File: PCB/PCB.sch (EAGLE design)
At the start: 216 parts, among them J3 Boot, Q1 FS8205A, U1 ESP32-S3HOLE

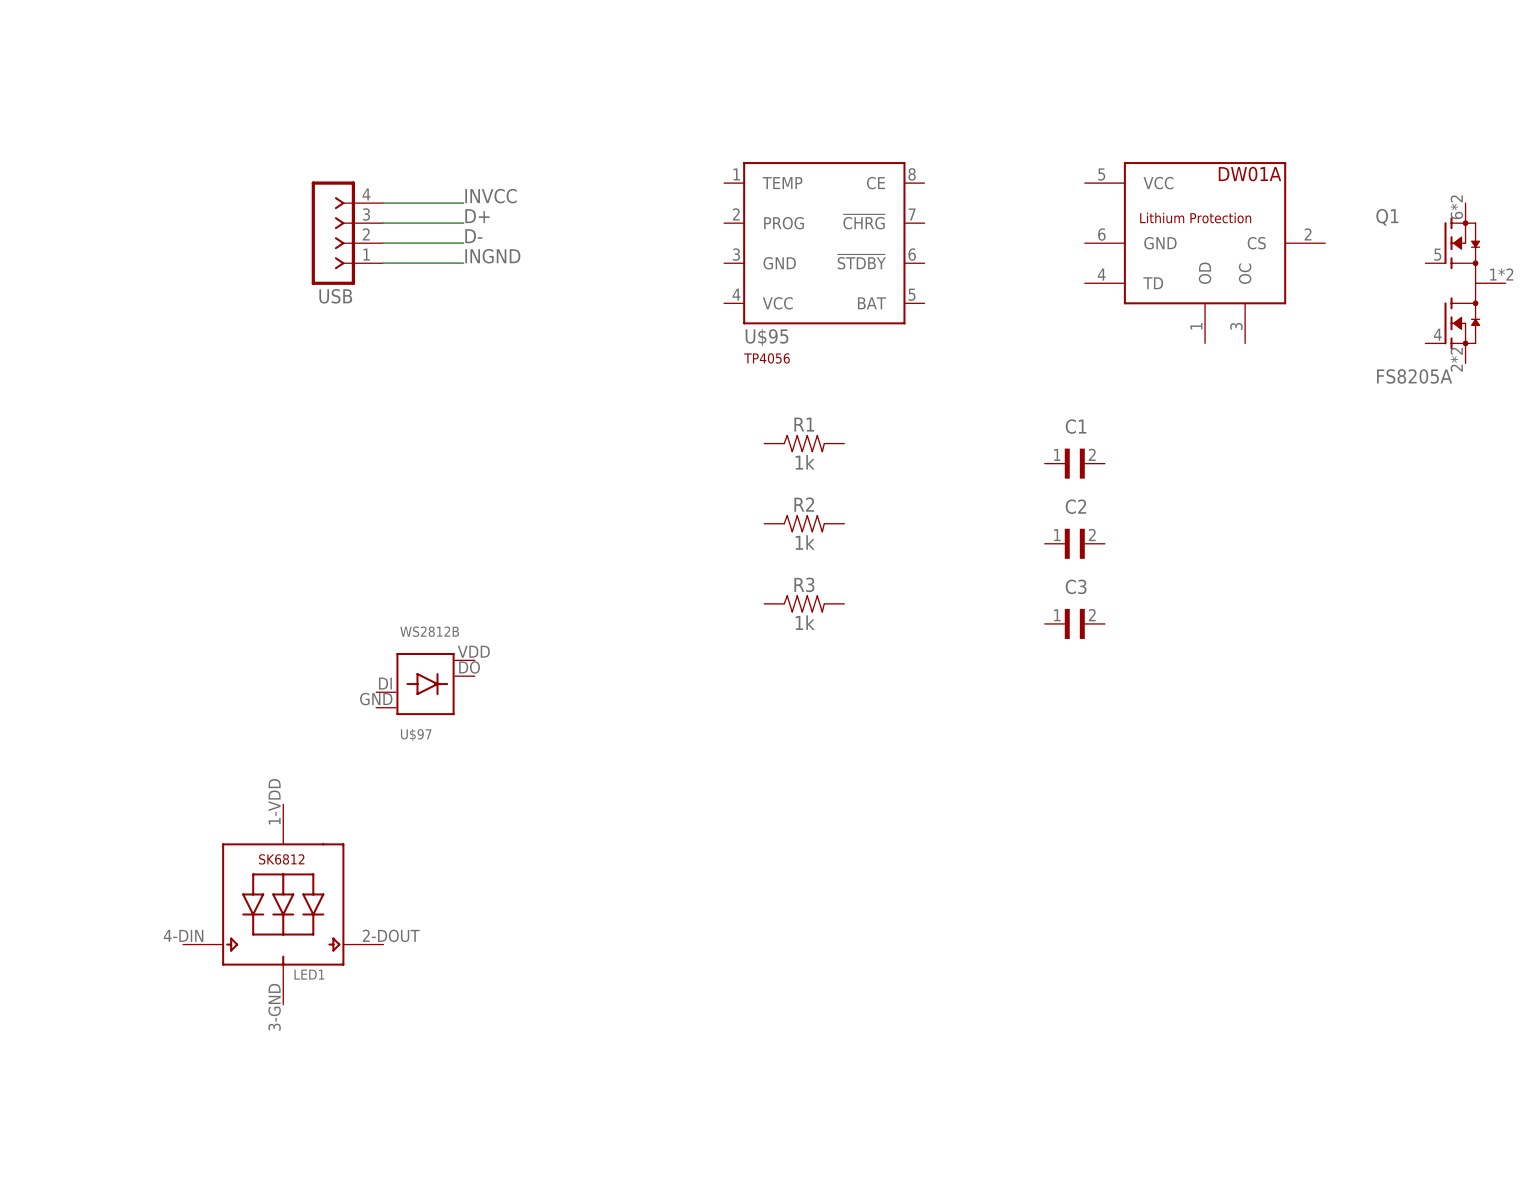
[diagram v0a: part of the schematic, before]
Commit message: Make the connections for the Battery and Power circuits
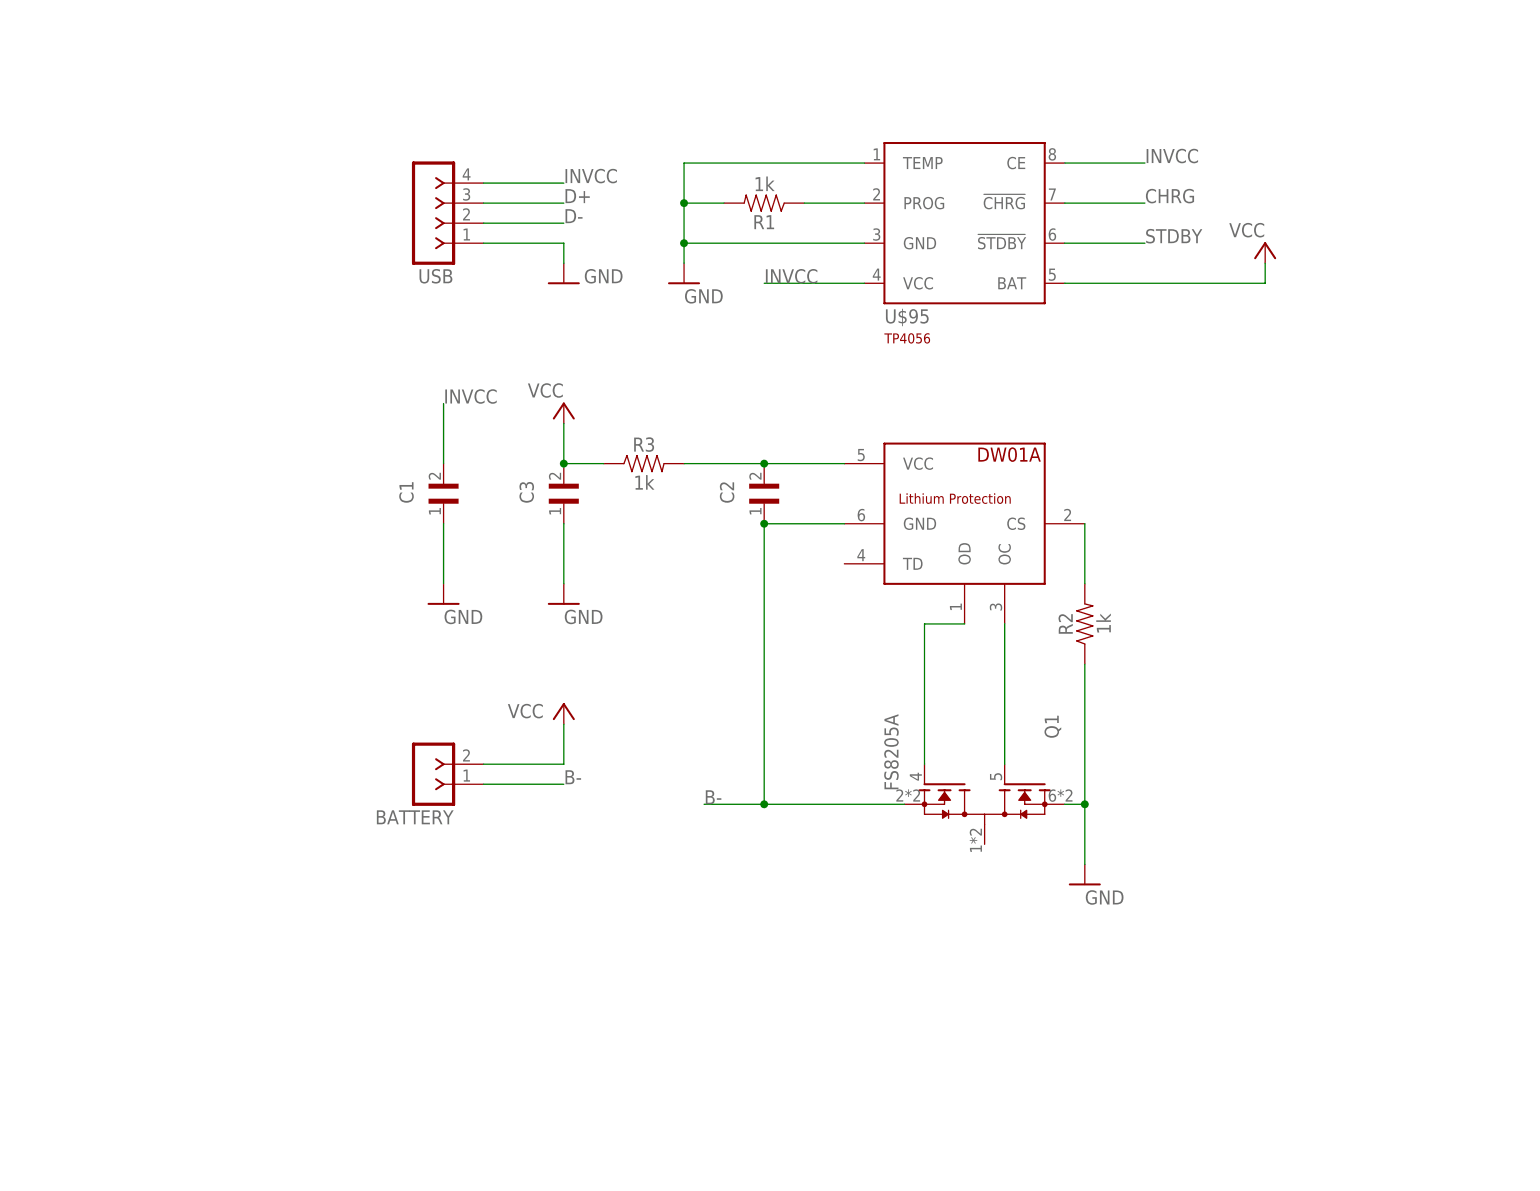
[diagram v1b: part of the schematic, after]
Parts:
- removed LED1: (no value), SMD5050 LED:SK6812_5050W
- removed U$97: WS2812B, Led-WS2812B:WS2812B
- added BATTERY: F-1X02-SIP-100-40, con-headers-jp:F-1X02-SIP-100-40
- C1, C2, C3: value RDE5C1H273J2M1H03A -> 1uF
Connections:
- removed net INGND: USB.1
- new net B-: BATTERY.1, C2.1, Q1.S1, U$96.GND
- new net CHRG: U$95.!CHRG
- new net N$31: R1.1, U$95.PROG
- new net N$32: R2.2, U$96.CS
- new net N$33: Q1.G2, U$96.OC
- new net N$34: Q1.G1, U$96.OD
- new net N$36: C2.2, R3.2, U$96.VCC
- new net STDBY: U$95.!STDBY
- net GND: now also C1.1, C3.1, Q1.S2, R1.2, R2.1, U$95.GND, U$95.TEMP, USB.1
- net INVCC: now also C1.2, U$95.CE, U$95.VCC
- net VCC: now also BATTERY.2, C3.2, R3.1, U$95.BAT
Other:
- moved on the sheet: C1, C2, C3, Q1, R1, R2, R3, U$95, USB

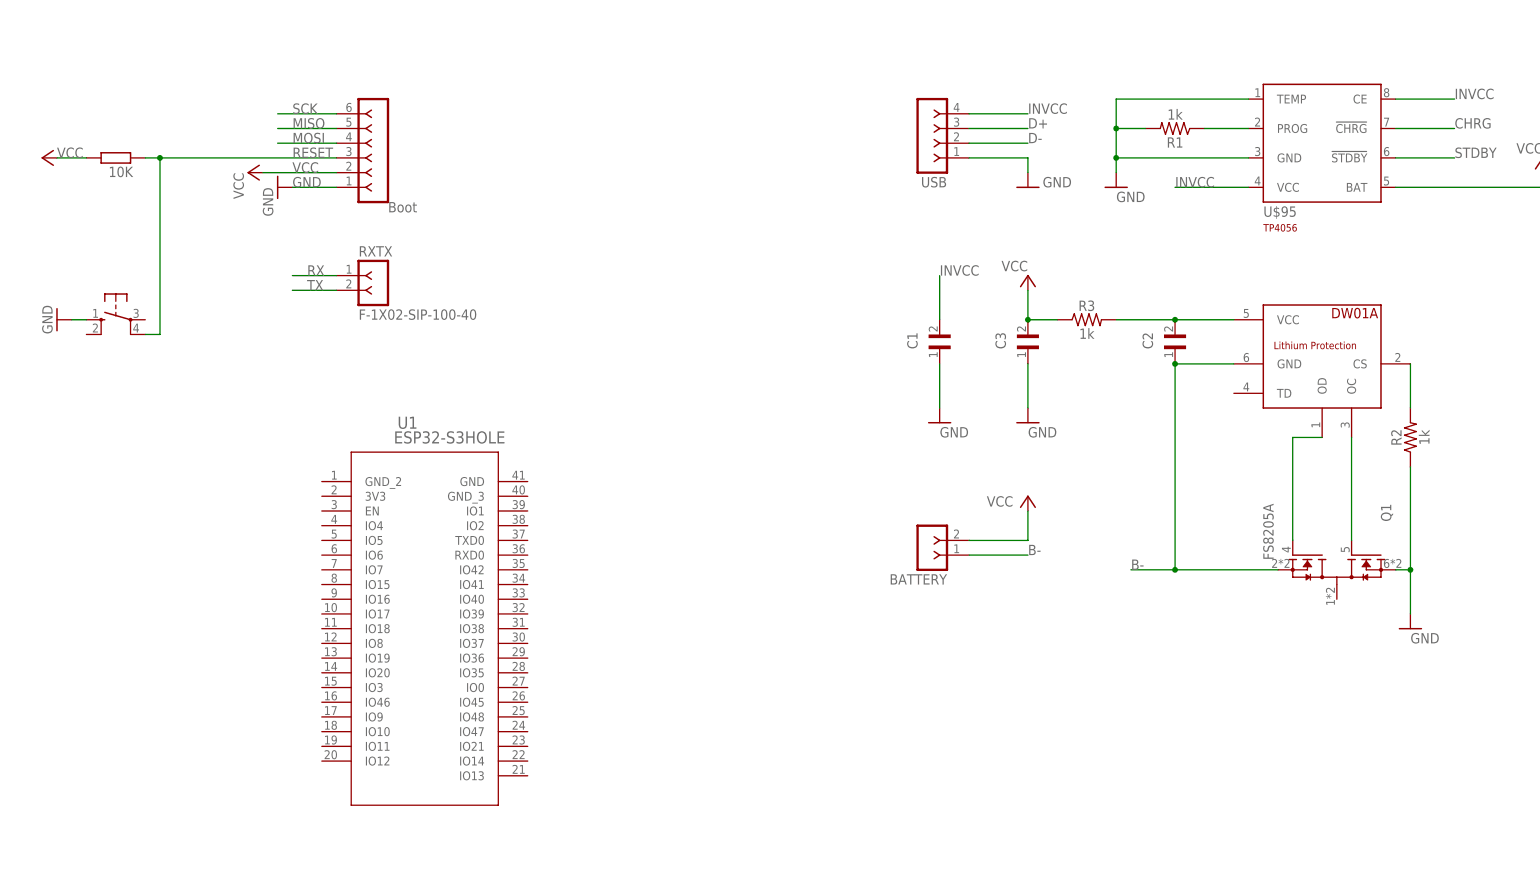
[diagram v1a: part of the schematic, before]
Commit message: Changed Capacitor and resistor type
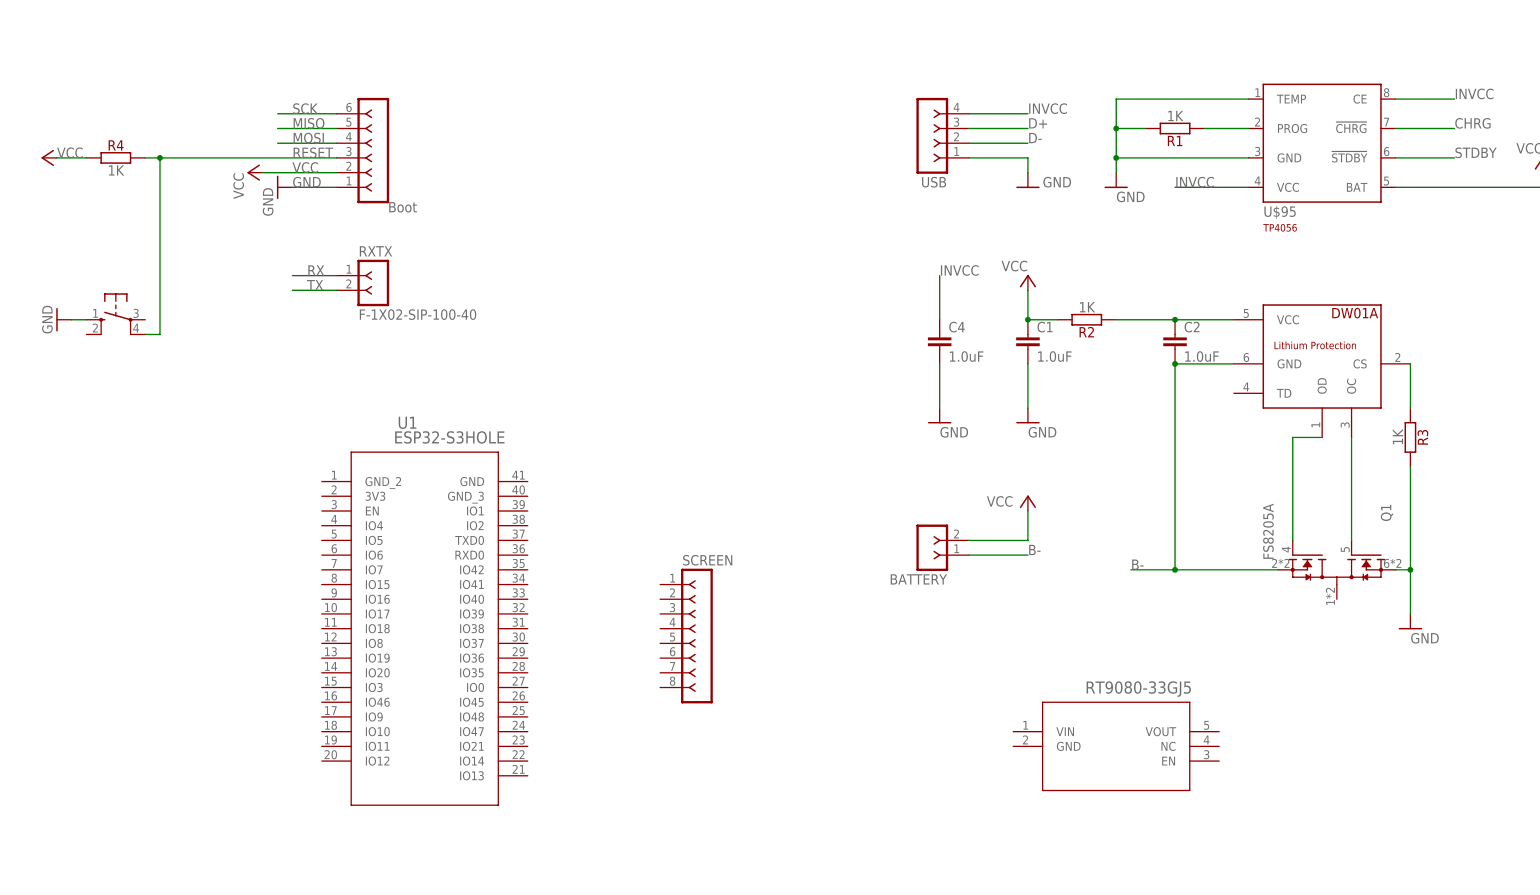
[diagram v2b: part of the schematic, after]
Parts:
- removed C3: 1uF, Capacitor:RDE5C1H273J2M1H03A
- removed R5: 10K, rcl:R-EU_0204/7
- added C4: 1.0uF, SparkFun-Capacitors:1.0UF-1206-50V-10%
- added R4: 1K, resistors:1K
- added REGULATOR: RT9080-33GJ5, RT9080:RT9080-33GJ5
- added SCREEN: F-1X08-SIP-100-40, con-headers-jp:F-1X08-SIP-100-40
- C1, C2: value 1uF -> 1.0uF; device Capacitor:RDE5C1H273J2M1H03A -> SparkFun-Capacitors:1.0UF-1206-50V-10%
- R1, R2, R3: value 1k -> 1K; device SparkFun-Resistors:100OHM-HORIZ_KIT-1/4W-1% -> resistors:1K
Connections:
- net B-: now also C2.2; no longer C2.1
- net GND: now also C1.2, C4.2, R3.2; no longer C1.1, C3.1, R2.1
- net INVCC: now also C4.1; no longer C1.2
- net N$32: now also R3.1; no longer R2.2
- net N$36: now also C2.1, R2.1; no longer C2.2, R3.2
- net RESET: now also R4.2; no longer R5.2
- net VCC: now also C1.1, R2.2, R4.1; no longer C3.2, R3.1, R5.1
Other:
- moved on the sheet: C1, C2

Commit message: Added the esp32 chip connections lines in .sch
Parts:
- removed D89: (no value), bt_diode:ZENER-DIODE-SOD123
- removed U$67: CHERRY-MX, cherrymx:CHERRY-MX
- added FN_KEY: CHERRY-MX, cherrymx:CHERRY-MX
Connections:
- removed net N$79: D89.C, U$67.PIN-2
- new net BATLEVEL: U1.IO1
- new net BLK: SCREEN.8, U1.IO47
- new net CS: SCREEN.7, U1.IO38
- new net DC: SCREEN.6, U1.IO39
- new net EN: U1.EN
- new net KEY_FN: FN_KEY.PIN-2, U1.IO10
- new net LEDS: U1.IO48
- new net PROG: U1.IO0
- new net RES: SCREEN.5, U1.IO40
- new net SCL: SCREEN.3, U1.IO42
- new net SDA: SCREEN.4, U1.IO41
- net CHRG: now also U1.IO2
- net COD0: now also U1.IO4
- net COD1: now also U1.IO5
- net COD2: now also U1.IO6
- net COD3: now also U1.IO7
- net E0: now also U1.IO15
- net E1: now also U1.IO16
- net E2: now also U1.IO17
- net E3: now also U1.IO18
- net E4: now also U1.IO8
- net E5: now also U1.IO9; no longer D89.A
- net GND: now also FN_KEY.PIN-1, SCREEN.1, U1.GND, U1.GND_2, U1.GND_3
- net MUX11: no longer U$67.PIN-1
- net RX: now also U1.RXD0
- net TX: now also U1.TXD0
- net VCC: now also SCREEN.2, U1.3V3
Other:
- moved on the sheet: BATTERY, C1, C2, C4, Q1, R1, R2, R3, R4, RXTX, SCREEN, U$95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
